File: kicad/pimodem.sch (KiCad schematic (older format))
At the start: 36 parts, among them J1 PWR_HEADER, J2 PI_HEADER, J3 SERIAL, J4 AUDIO_HEADER, J5 LED_PANEL, J6 WP, J7 GAIN, Q1 DMG2305UX, Q2 BC857BS, Q3 DMG3414U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

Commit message: Update kicad schematic to latest version of kicad nightly
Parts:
- C1, C2, C3, C4, C5, C6, C7, C8, C9: symbol C_Small -> Device:C_Small
- D1: symbol TVS -> pimodem:TVS
- F1: symbol Polyfuse -> Device:Polyfuse
- J1: symbol CONN_02X03 -> Connector_Generic:Conn_02x03_Odd_Even
- J2: symbol CONN_02X20 -> Connector_Generic:Conn_02x20_Odd_Even
- J3, J5: symbol CONN_02X05 -> Connector_Generic:Conn_02x05_Odd_Even
- J4: symbol CONN_01X07 -> Connector_Generic:Conn_01x07
- J6: symbol CONN_01X02 -> Connector_Generic:Conn_01x02
- J7: symbol CONN_02X04 -> Connector_Generic:Conn_02x04_Odd_Even
- Q1: symbol Q_PMOS_GSD -> Device:Q_PMOS_GSD
- Q2: footprint TO_SOT_Packages_SMD:SOT-363 -> Package_TO_SOT_SMD:SOT-363_SC-70-6; symbol BC857BS -> Transistor_BJT:BC857BS
- Q2: footprint TO_SOT_Packages_SMD:SOT-363_SC-70-6 -> Package_TO_SOT_SMD:SOT-363_SC-70-6; symbol BC857BS -> Transistor_BJT:BC857BS
- Q3: symbol Q_NMOS_GSD -> Device:Q_NMOS_GSD
- R1, R2, R3, R4, R5, R6, R7, R8, R9: symbol R -> Device:R
- U1: symbol LTC2951 -> pimodem:LTC2951
- U2: symbol LTC4360 -> pimodem:LTC4360
- U3: symbol ULN2803A -> Transistor_Array:ULN2803A
- U4: symbol MAX3237 -> pimodem:MAX3237
- U5: symbol 74LS04 -> pimodem:74LS04
- U6: symbol 24LC32 -> Memory_EEPROM:24LC32
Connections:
- wire segments 214 -> 257
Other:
- note removed: "1.0\n"
- note removed: "8-10-17"
- note removed: "PiModem"

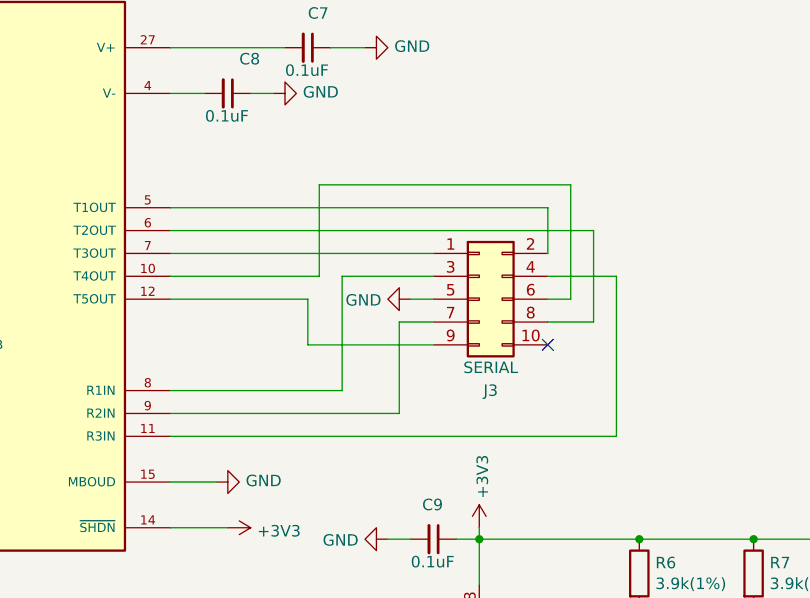
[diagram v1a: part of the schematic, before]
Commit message: Update traces for serial header to use DTK/intel format
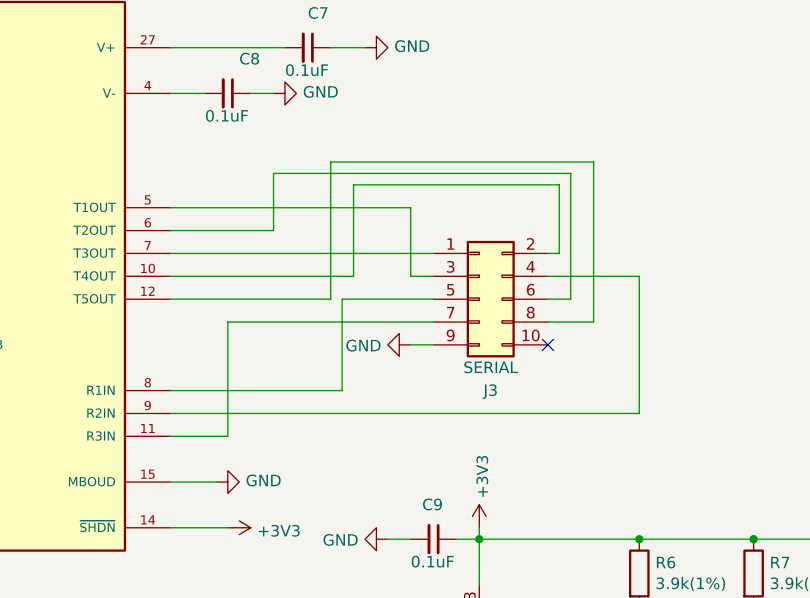
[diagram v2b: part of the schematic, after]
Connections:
- net GND: now also J3.9 (Pin_9); no longer J3.5 (Pin_5)
- net at U4.10 (T4OUT): now also J3.2 (Pin_2); no longer J3.6 (Pin_6)
- net at U4.11 (R3IN): now also J3.7 (Pin_7); no longer J3.4 (Pin_4)
- net at U4.12 (T5OUT): now also J3.8 (Pin_8); no longer J3.9 (Pin_9)
- net at U4.5 (T1OUT): now also J3.3 (Pin_3); no longer J3.2 (Pin_2)
- net at U4.6 (T2OUT): now also J3.6 (Pin_6); no longer J3.8 (Pin_8)
- net at U4.8 (R1IN): now also J3.5 (Pin_5); no longer J3.3 (Pin_3)
- net at U4.9 (R2IN): now also J3.4 (Pin_4); no longer J3.7 (Pin_7)
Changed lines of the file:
@@
 Title "PiModem"
 Date "08/10/17"
-Rev "1.0"
+Rev "1.1"
 Comp ""
 Comment1 ""
@@
 L power:GND #PWR025
 U 1 1 598805E5
-P 3450 5500
-F 0 "#PWR025" H 3450 5250 50  0001 C CNN
-F 1 "GND" V 3455 5372 50  0000 R CNN
-F 2 "" H 3450 5500 50  0001 C CNN
-F 3 "" H 3450 5500 50  0001 C CNN
-	1    3450 5500
+P 3450 5700
+F 0 "#PWR025" H 3450 5450 50  0001 C CNN
+F 1 "GND" V 3455 5572 50  0000 R CNN
+F 2 "" H 3450 5700 50  0001 C CNN
+F 3 "" H 3450 5700 50  0001 C CNN
+	1    3450 5700
 	0    1    1    0
 $EndComp
@@
 	900  5500 1200 5500
 Wire Wire Line
-	3450 5500 3550 5500
+	3450 5700 3550 5700
 Wire Wire Line
 	2400 5300 3550 5300
 Wire Wire Line
-	2400 5100 4050 5100
-Wire Wire Line
-	4050 5100 4050 5300
-Wire Wire Line
 	2400 5900 3150 5900
-Wire Wire Line
-	3150 5900 3150 5400
-Wire Wire Line
-	3150 5400 3550 5400
-Wire Wire Line
-	2400 6100 4350 6100
-Wire Wire Line
-	4350 6100 4350 5400
-Wire Wire Line
-	4350 5400 4050 5400
-Wire Wire Line
-	2400 5400 3050 5400
-Wire Wire Line
-	3050 5400 3050 5000
-Wire Wire Line
-	3050 5000 4150 5000
-Wire Wire Line
-	4150 5000 4150 5500
-Wire Wire Line
-	4150 5500 4050 5500
-Wire Wire Line
-	2400 6000 3400 6000
-Wire Wire Line
-	3400 6000 3400 5600
-Wire Wire Line
-	3400 5600 3550 5600
-Wire Wire Line
-	2400 5200 4250 5200
-Wire Wire Line
-	4250 5200 4250 5600
-Wire Wire Line
-	4250 5600 4050 5600
-Wire Wire Line
-	2400 5500 3000 5500
-Wire Wire Line
-	3000 5500 3000 5700
-Wire Wire Line
-	3000 5700 3550 5700
 Wire Wire Line
 	9900 2600 10200 2600
@@
 	8800 3800 8800 3700
 Connection ~ 8800 3700
+Wire Wire Line
+	2400 5100 3450 5100
+Wire Wire Line
+	3450 5100 3450 5400
+Wire Wire Line
+	3450 5400 3550 5400
+Wire Wire Line
+	3550 5500 3150 5500
+Wire Wire Line
+	3150 5500 3150 5900
+Wire Wire Line
+	3550 5600 2650 5600
+Wire Wire Line
+	2650 5600 2650 6100
+Wire Wire Line
+	2650 6100 2400 6100
+Wire Wire Line
+	3200 5400 3200 5000
+Wire Wire Line
+	3200 5000 4100 5000
+Wire Wire Line
+	4100 5000 4100 5300
+Wire Wire Line
+	4100 5300 4050 5300
+Wire Wire Line
+	2400 5400 3200 5400
+Wire Wire Line
+	4050 5400 4450 5400
+Wire Wire Line
+	4450 5400 4450 6000
+Wire Wire Line
+	2400 6000 4450 6000
+Wire Wire Line
+	4050 5500 4150 5500
+Wire Wire Line
+	4150 5500 4150 4950
+Wire Wire Line
+	4150 4950 2850 4950
+Wire Wire Line
+	2850 4950 2850 5200
+Wire Wire Line
+	2850 5200 2400 5200
+Wire Wire Line
+	3100 5500 3100 4900
+Wire Wire Line
+	3100 4900 4250 4900
+Wire Wire Line
+	4250 4900 4250 5600
+Wire Wire Line
+	4250 5600 4050 5600
+Wire Wire Line
+	2400 5500 3100 5500
 $EndSCHEMATC

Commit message: kicad: update schematic to use 128kbit eeprom
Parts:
- U6: value 24LC32 -> 24LC128; symbol Memory_EEPROM:24LC32 -> Memory_EEPROM:24LC128; Digikey CAT24C32WI-GOS-ND -> CAT24C128WI-GT3CT-ND; MFN CAT24C32WI-G -> CAT24C128WI-GT
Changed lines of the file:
@@
 $EndComp
 $Comp
-L Memory_EEPROM:24LC32 U6
+L Memory_EEPROM:24LC128 U6
 U 1 1 598902DA
 P 3750 7050
 F 0 "U6" H 3600 6800 50  0000 C CNN
-F 1 "24LC32" H 3900 6800 50  0000 C CNN
+F 1 "24LC128" H 3900 6800 50  0000 C CNN
 F 2 "Housings_SOIC:SOIC-8_3.9x4.9mm_Pitch1.27mm" H 3800 6800 50  0001 L CNN
 F 3 "http://www.onsemi.com/pub/Collateral/CAT24C32-D.PDF" H 3750 6950 50  0001 C CNN
-F 4 "CAT24C32WI-G" H 3750 7050 60  0001 C CNN "MFN"
-F 5 "CAT24C32WI-GOS-ND" H 3750 7050 60  0001 C CNN "Digikey"
+F 4 "CAT24C128WI-GT" H 3750 7050 60  0001 C CNN "MFN"
+F 5 "CAT24C128WI-GT3CT-ND" H 3750 7050 60  0001 C CNN "Digikey"
 	1    3750 7050
 	1    0    0    -1

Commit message: kicad: Update schematic and pcb layout
* Connect serial gpio signals through inverter gates
* Connect all leds to gpio pins
* Update eeprom to 24c512
* Update pcb footprints to new names (kicad update)
* Update schematic/board revision to 1.2
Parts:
- removed J6: WP, Pin_Headers:Pin_Header_Straight_1x02_Pitch2.54mm, symbol Connector_Generic:Conn_01x02
- added R10: 0Ohm, Resistor_SMD:R_0805_2012Metric, symbol Device:R
- C1, C2, C3, C4, C5, C6, C7, C8, C9: footprint Capacitors_SMD:C_0805 -> Capacitor_SMD:C_0805_2012Metric
- D1: footprint Diodes_SMD:D_SMB_Standard -> Diode_SMD:D_SMB
- F1: footprint Resistors_SMD:R_1812 -> Resistor_SMD:R_1812_4532Metric
- J1: footprint Connectors_Molex:Molex_Microfit3_Header_02x03_Straight_43045-0628 -> Connector_Molex:Molex_Micro-Fit_3.0_43045-0612_2x03_P3.00mm_Vertical
- J2: footprint Socket_Strips:Socket_Strip_Straight_2x20_Pitch2.54mm -> Connector_PinSocket_2.54mm:PinSocket_2x20_P2.54mm_Vertical
- J3, J5: footprint Pin_Headers:Pin_Header_Straight_2x05_Pitch2.54mm -> Connector_PinHeader_2.54mm:PinHeader_2x05_P2.54mm_Vertical
- J7: footprint Pin_Headers:Pin_Header_Straight_2x04_Pitch2.54mm -> Connector_PinHeader_2.54mm:PinHeader_2x04_P2.54mm_Vertical
- Q1, Q3: footprint TO_SOT_Packages_SMD:SOT-23 -> Package_TO_SOT_SMD:SOT-23
- R1, R2, R3, R4, R5, R6, R7, R8, R9: footprint Resistors_SMD:R_0805 -> Resistor_SMD:R_0805_2012Metric
- U1: footprint TO_SOT_Packages_SMD:SOT-23-8 -> Package_TO_SOT_SMD:SOT-23-8
- U2: footprint TO_SOT_Packages_SMD:SC-70-8 -> Package_TO_SOT_SMD:SC-70-8
- U3: footprint Housings_SOIC:SOIC-18W_7.5x11.6mm_Pitch1.27mm -> Package_SO:SOIC-18W_7.5x11.6mm_P1.27mm
- U4: footprint Housings_SSOP:SSOP-28_5.3x10.2mm_Pitch0.65mm -> Package_SO:SSOP-28_5.3x10.2mm_P0.65mm
- U5: footprint Housings_SOIC:SOIC-14_3.9x8.7mm_Pitch1.27mm -> Package_SO:SOIC-14_3.9x8.7mm_P1.27mm
- U6: value 24LC128 -> 24LC512; footprint Housings_SOIC:SOIC-8_3.9x4.9mm_Pitch1.27mm -> Package_SO:SOIC-8_3.9x4.9mm_P1.27mm; symbol Memory_EEPROM:24LC128 -> Memory_EEPROM:24LC512; Digikey CAT24C128WI-GT3CT-ND -> CAT24C512WI-GT3OSCT-ND; MFN CAT24C128WI-GT -> CAT24C512WI-GT3
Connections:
- net LED4 is gone; now on net DSR: U3.4 (I4)
- net LED5 is gone; now on net OH: U3.5 (I5)
- net LED6 is gone; now on net AA: U3.6 (I6)
- net DSR: now also U5.11; no longer U3.1 (I1), U4.19 (T4IN)
- net DTR: now also U3.3 (I3), U5.12; no longer U4.18 (R3OUT)
- net GND: now also R10.2; no longer U5.11, U5.13, U5.5, U5.9
- net RI: now also U5.9; no longer U4.17 (T5IN)
- net AA: now reaches J2.13 (Pin_13)
- net OH: now reaches J2.15 (Pin_15)
- net at U5.6: now also U4.22 (T3IN)
- net at U5.8: now also U4.17 (T5IN)
- net at U5.10: now also U4.19 (T4IN)
- net at R5.2, U6.7 (WP): now also R10.1
- removed net DCD: J2.29 (Pin_29), U3.3 (I3), U4.22 (T3IN)
- net LED2 renamed ACT
- net LED7 renamed SD
- net LED8 renamed RD
- new net: U4.18 (R3OUT), U5.13
- new net CD: J2.29 (Pin_29), U3.1 (I1), U5.5
- no-connect marks 24 -> 15
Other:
- moved on the sheet: C5, C6, C7, C8, C9, J3, R5, R6, R7, U4, U5C, U5D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
